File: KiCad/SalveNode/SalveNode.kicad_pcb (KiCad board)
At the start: 2 copper layers, 8 parts, among them IC1 DS89C21TMX_NOPB, IC2 TMP75AQDGKRQ1, IC3 ATMEGA328PB-AN, J1 Screw_Terminal_01x06, J2 Screw_Terminal_01x06

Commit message: pcb
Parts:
- added C1: C, Capacitor_SMD:C_1206_3216Metric_Pad1.33x1.80mm_HandSolder, F.Cu at (169.2, 56.6)
- added C2: C, Capacitor_SMD:C_1206_3216Metric_Pad1.33x1.80mm_HandSolder, F.Cu at (164.1, 56.6)
- added Y1: Crystal, Crystal:Crystal_HC18-U_Vertical, F.Cu at (169.1, 60.7)
- moved J1 66.7 mm to (180.1, 65.0), turned to 90 degrees
- moved IC3 62.6 mm to (166.6, 47.6), turned to 45 degrees
- moved A1 57.4 mm to (165.8, 39.5)
- moved IC2 56.2 mm to (158.3, 42.0), turned to 180 degrees
- moved R1 54.8 mm to (169.8, 39.5)
- moved J2 47.3 mm to (147.7, 40.0), turned to -90 degrees
- moved IC1 41.7 mm to (157.2, 54.4), turned to 180 degrees
- moved R2 40.2 mm to (156.1, 50.4), turned to 180 degrees
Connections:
- net /D0_1 renamed /D0-
- net /D0_2 renamed /D0+
- net /RI_1 renamed /RI-
- net /RI_2 renamed /RI+
- IC3 pad 7: unconnected-(IC3-(XTAL1/TOSC1)_PB6-Pad7) -> /XTAL1
- IC3 pad 8: unconnected-(IC3-(XTAL2/TOSC2)_PB7-Pad8) -> /XTAL2
- R1 pad 2: +5V -> Earth
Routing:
- net /RI+: track 0.00 -> 15.8 mm
- net /RI-: track 0.00 -> 15.6 mm
- net /MOSI: track 0.00 -> 14.5 mm
- net /RX: track 0.00 -> 14.1 mm
- net /XTAL2: track 0.00 -> 12.6 mm
- net /D0+: track 0.00 -> 12.4 mm
- net /D0-: track 0.00 -> 11.9 mm
- net /TX: track 0.00 -> 11.2 mm
- net /MISO: track 0.00 -> 11.1 mm
- net /XTAL1: track 0.00 -> 10.4 mm
- net /SCK: track 0.00 -> 9.15 mm
- net /SCL: track 0.00 -> 6.99 mm
- net /LIGHT_IN: track 0.00 -> 5.83 mm
- net /SDA: track 0.00 -> 4.27 mm
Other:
- board outline added: 42.6 x 31.1 mm
- board text added: "+5"
- board text added: "GND"
- board text added: "MISO"
- board text added: "MOSI"
- board text added: "RESET"
- board text added: "SCK"

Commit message: pcb changes
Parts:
- added C3: 100n, Capacitor_SMD:C_1206_3216Metric_Pad1.33x1.80mm_HandSolder, F.Cu at (188.8, 44.3)
- added C4: 100n, Capacitor_SMD:C_1206_3216Metric_Pad1.33x1.80mm_HandSolder, F.Cu at (188.8, 47.7)
- added C5: 100n, Capacitor_SMD:C_1206_3216Metric_Pad1.33x1.80mm_HandSolder, F.Cu at (188.8, 51.0)
- added C6: 100n, Capacitor_SMD:C_1206_3216Metric_Pad1.33x1.80mm_HandSolder, F.Cu at (188.8, 54.4)
- added C7: 100n, Capacitor_SMD:C_1206_3216Metric_Pad1.33x1.80mm_HandSolder, F.Cu at (188.8, 57.7)
- added IC4: VEML7700-TR, SamacSys_Parts:VEML7700, F.Cu at (192.6, 46.5)
- added R3: PAD, Resistor_SMD:R_1206_3216Metric_Pad1.30x1.75mm_HandSolder, F.Cu at (194.8, 49.8)
- added R4: PAD, Resistor_SMD:R_1206_3216Metric_Pad1.30x1.75mm_HandSolder, F.Cu at (194.8, 53.1)
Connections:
- J1 pad 1: +5V -> Earth
- J1 pad 4: /RESET -> /SCK
- J1 pad 5: /SCK -> /RESET
- J1 pad 6: Earth -> +5V
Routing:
- net /RI+: track 15.8 -> 0.00 mm
- net /RI-: track 15.6 -> 0.00 mm
- net /MOSI: track 14.5 -> 0.00 mm
- net /RX: track 14.1 -> 0.00 mm
- net /XTAL2: track 12.6 -> 0.00 mm
- net /D0+: track 12.4 -> 0.00 mm
- net /D0-: track 11.9 -> 0.00 mm
- net /TX: track 11.2 -> 0.00 mm
- net /MISO: track 11.1 -> 0.00 mm
- net /XTAL1: track 10.4 -> 0.00 mm
- net /SCK: track 9.15 -> 0.00 mm
- net /SCL: track 6.99 -> 0.00 mm
- net /LIGHT_IN: track 5.83 -> 0.00 mm
- net /SDA: track 4.27 -> 0.00 mm

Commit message: PCB Complete
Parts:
- removed A1: ALS-PT19-315C_L177_TR8, SimbolosSnapEDA:XDCR_ALS-PT19-315C_L177_TR8
- removed the IC3 at (166.6, 47.6)
- added R2: R, Resistor_SMD:R_1206_3216Metric_Pad1.30x1.75mm_HandSolder, F.Cu at (133.3, 50.9)
- added U1: ATmega328PB-A, Package_QFP:TQFP-32_7x7mm_P0.8mm, F.Cu at (147.7, 55.0)
- R1: value 10k -> R
- moved R5 59.6 mm to (136.1, 42.6), turned to 90 degrees
- moved R4 58.9 mm to (136.1, 55.0), turned to 90 degrees
- moved C7 58.6 mm to (130.9, 48.2), turned to 90 degrees
- moved IC3 56.1 mm to (136.5, 45.4), turned to -90 degrees
- moved C5 55.3 mm to (135.4, 65.7)
- moved C4 48.1 mm to (142.0, 58.6), turned to 135 degrees
- moved C6 45.2 mm to (144.3, 46.1), turned to 180 degrees
- moved R1 37.0 mm to (133.3, 45.9), turned to -90 degrees
- moved C3 36.7 mm to (152.6, 50.1), turned to -45 degrees
- moved R3 29.5 mm to (129.3, 62.9), turned to 90 degrees
- moved J2 25.5 mm to (122.3, 43.1)
- moved IC1 23.9 mm to (134.5, 61.6)
- moved C1 22.2 mm to (148.2, 64.1)
- moved Y1 22.2 mm to (148.2, 68.2)
- moved C2 22.2 mm to (143.2, 64.1)
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- renumbered IC4 to IC3, R2 to R3, R3 to R4, R4 to R5
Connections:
- IC2 pad 5: Earth -> +5V
- IC2 pad 6: Earth -> +5V
- IC2 pad 7: Earth -> +5V
- IC3 pad 2: Net-(IC4-VDD) -> Net-(IC3-VDD)
- R1 pad 1: /LIGHT_IN -> +5V
- R1 pad 2: Earth -> Net-(IC3-VDD)
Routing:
- net Earth: track 0.00 -> 116.2 mm, vias 0 -> 4
- net +5V: track 0.00 -> 108.6 mm
- net /SCL: track 0.00 -> 23.9 mm
- net /RESET: track 0.00 -> 22.9 mm, vias 0 -> 1
- net /SDA: track 0.00 -> 22.8 mm, vias 0 -> 2
- net /RX: track 0.00 -> 17.3 mm
- net /D0+: track 0.00 -> 15.6 mm
- net /D0-: track 0.00 -> 15.5 mm
- net /MOSI: track 0.00 -> 13.8 mm
- net /RI+: track 0.00 -> 13.3 mm
- net /RI-: track 0.00 -> 13.3 mm
- net /TX: track 0.00 -> 12.4 mm
- net /MISO: track 0.00 -> 11.4 mm
- net /XTAL1: track 0.00 -> 11.4 mm
- net /SCK: track 0.00 -> 10.9 mm
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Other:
- board size 42.6 x 31.1 mm -> 51.2 x 31 mm

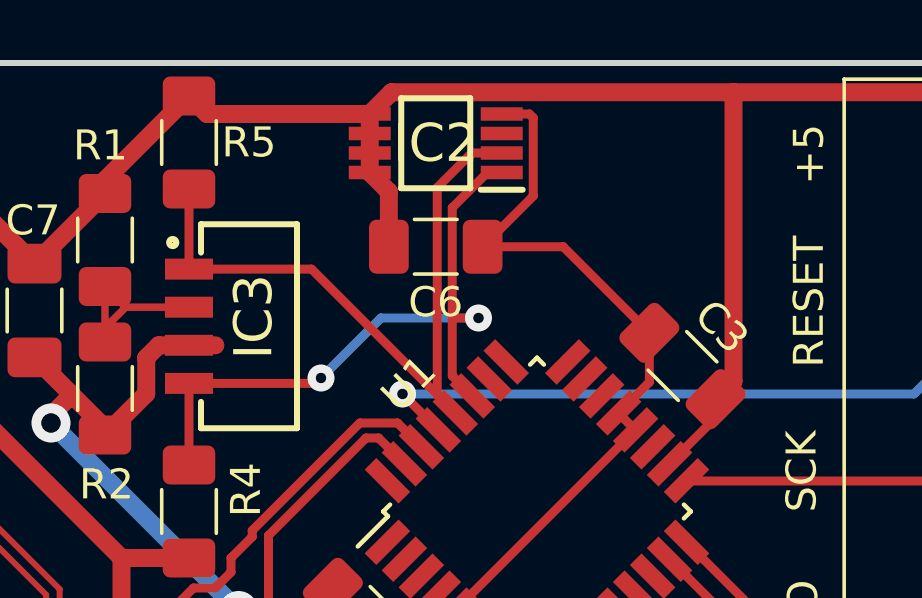
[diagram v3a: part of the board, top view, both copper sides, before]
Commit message: fixed missing R for reset while programming
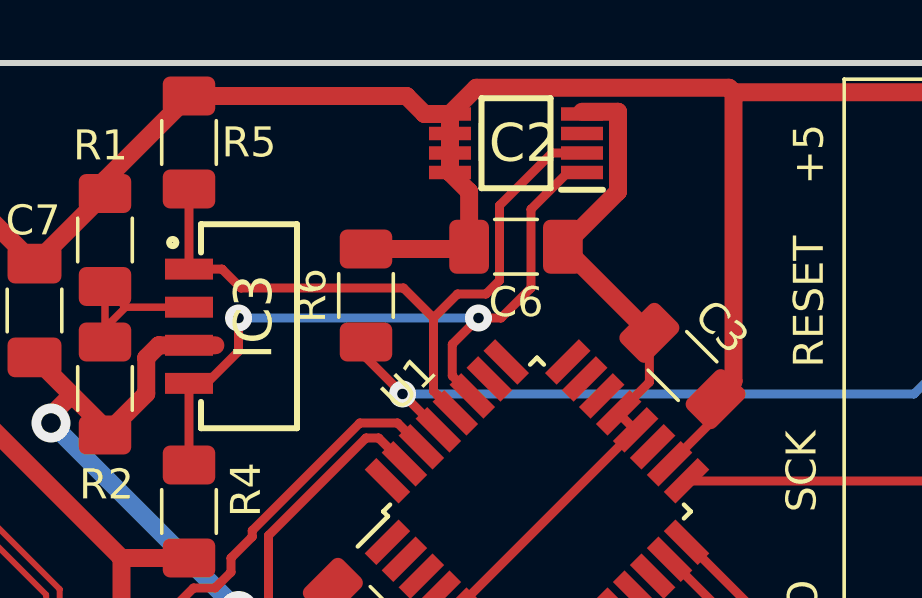
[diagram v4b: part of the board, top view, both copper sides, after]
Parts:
- added R6: PAD, Resistor_SMD:R_1206_3216Metric_Pad1.30x1.75mm_HandSolder, F.Cu at (142.0, 47.8)
- moved C6 2.68 mm to (147.0, 46.1)
- moved IC2 2.68 mm to (147.0, 42.7)
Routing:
- net +5V: track 108.6 -> 112.2 mm
- net Earth: track 116.2 -> 113.9 mm
- net /RESET: track 22.9 -> 25.1 mm
- net /SDA: track 22.8 -> 24.2 mm
- net /SCL: track 23.9 -> 24.5 mm

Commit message: Created Arduino Files for Node + fixed missing pullup resistor for ALERT pin in tmp75
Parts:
- added R7: 5k, Resistor_SMD:R_1206_3216Metric_Pad1.30x1.75mm_HandSolder, F.Cu at (155.0, 44.0)
- R1: value R -> 1k
- R2: value R -> 2k
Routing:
- net unconnected-(IC2-ALERT-Pad3): track 0.00 -> 6.30 mm
- net Earth: track 113.9 -> 117.5 mm, vias 4 -> 6
- net +5V: track 112.2 -> 114.8 mm

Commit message: BOM
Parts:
- removed Y1: Crystal, Crystal:Crystal_HC18-U_Vertical
- added Y2: 16M, SamacSys_Parts:ECS1601036CKMTR3, F.Cu at (145.4, 67.1)
- C1, C2: value C -> 12p; footprint Capacitor_SMD:C_1206_3216Metric_Pad1.33x1.80mm_HandSolder -> Capacitor_SMD:C_1206_3216Metric
- C3, C4, C5, C6, C7: footprint Capacitor_SMD:C_1206_3216Metric_Pad1.33x1.80mm_HandSolder -> Capacitor_SMD:C_1206_3216Metric
- R1, R2, R3, R6, R7: footprint Resistor_SMD:R_1206_3216Metric_Pad1.30x1.75mm_HandSolder -> Resistor_SMD:R_1206_3216Metric
- moved C2 0.56 mm to (142.8, 64.5), turned to 45 degrees
- moved C1 0.45 mm to (148.0, 64.5), turned to 135 degrees
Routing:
- net Earth: track 117.5 -> 120.2 mm
- net /XTAL1: track 11.4 -> 8.75 mm
- net /XTAL2: track 10.2 -> 7.71 mm

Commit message: BOM and PCB updated
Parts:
- removed J1: Screw_Terminal_01x06, TerminalBlock_Phoenix:TerminalBlock_Phoenix_MKDS-1,5-6_1x06_P5.00mm_Horizontal
- added J3: 691382040006, SimbolosSnapEDA:691382040006, F.Cu at (126.5, 55.2)
- J2: value Screw_Terminal_01x06 -> AVR-ISP-6; footprint TerminalBlock_Phoenix:TerminalBlock_Phoenix_MKDS-1,5-6_1x06_P5.00mm_Horizontal -> Connector_PinHeader_1.00mm:PinHeader_2x03_P1.00mm_Vertical
- R4, R5: footprint Resistor_SMD:R_1206_3216Metric_Pad1.30x1.75mm_HandSolder -> Resistor_SMD:R_1206_3216Metric
- R6: value PAD -> 10k
- moved J2 37.3 mm to (156.0, 59.2), turned to -45 degrees
- moved R5 0.18 mm to (136.0, 42.5)
- moved R4 0.11 mm to (136.0, 55.0)
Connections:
- J2 pad 1: +5V -> /MISO
- J2 pad 2: /D0- -> +5V
- J2 pad 3: /D0+ -> /SCK
- J2 pad 4: /RI- -> /MOSI
- J2 pad 5: /RI+ -> /RESET
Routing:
- net +5V: track 114.8 -> 105.7 mm
- net /MISO: track 11.4 -> 4.72 mm
- net /D0-: track 15.5 -> 10.4 mm
- net /RESET: track 25.1 -> 20.5 mm, vias 1 -> 2
- net /D0+: track 15.6 -> 11.5 mm
- net /RI-: track 13.3 -> 10.1 mm
- net /RI+: track 13.3 -> 10.2 mm
- net /MOSI: track 13.8 -> 15.3 mm
- net /SCK: track 10.9 -> 9.74 mm, vias 0 -> 2
- net Earth: track 120.2 -> 120.1 mm, vias 6 -> 7
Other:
- board size 51.2 x 31 mm -> 41.5 x 31 mm

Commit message: Production
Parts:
- removed the R1 at (133.3, 45.9)
- removed R2: 2k, Resistor_SMD:R_1206_3216Metric
- added C1: 1u, Capacitor_SMD:C_1206_3216Metric, F.Cu at (137.8, 42.8)
- added C9: 1u, Capacitor_SMD:C_1206_3216Metric, F.Cu at (130.5, 43.0)
- added U1: MCP1700x-330xxTT, Package_TO_SOT_SMD:SOT-23, F.Cu at (133.8, 42.5)
- J1: renamed from J2; footprint Connector_PinHeader_1.00mm:PinHeader_2x03_P1.00mm_Vertical -> Connector_PinHeader_2.54mm:PinHeader_2x03_P2.54mm_Vertical
- J3: value 691382040006 -> 691382030006; footprint SimbolosSnapEDA:691382040006 -> SimbolosSnapEDA:691382030006
- R6: renamed from R4; value PAD -> 4.7k
- R7: renamed from R5; value PAD -> 4.7k
- moved R7 6.01 mm to (142.0, 42.8)
- moved J3 3.50 mm to (123.0, 55.2)
- moved J1 0.22 mm to (155.9, 59.1)
- renumbered C1 to C2, C2 to C3, C3 to C4, C4 to C5, C5 to C6, C6 to C7, C7 to C8, R7 to R1, R6 to R4, R3 to R5, U1 to U2, Y2 to Y1
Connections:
- IC3 pad 2: Net-(IC3-VDD) -> +3.3V
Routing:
- net Earth: track 120.1 -> 59.6 mm, vias 7 -> 6
- net +5V: track 105.7 -> 117.7 mm
- net +3.3V: track 0.00 -> 9.83 mm
- net /MOSI: track 15.3 -> 7.67 mm
- net Net-(IC3-VDD): track 6.38 -> 0.00 mm
- net /RI-: track 10.1 -> 16.1 mm
- net /RI+: track 10.2 -> 15.6 mm
- net /SCK: track 9.74 -> 13.0 mm
- net /D0-: track 10.4 -> 13.6 mm
- net /D0+: track 11.5 -> 14.1 mm
- net /SCL: track 24.5 -> 26.0 mm
- net /SDA: track 24.2 -> 23.6 mm
- added copper zone on F.Cu, net Earth
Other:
- board size 41.5 x 31 mm -> 42.8 x 31 mm
